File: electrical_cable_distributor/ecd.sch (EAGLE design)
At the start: 4 parts, among them X1 DG300-5.0-03P-13-00AH, X2 DG300-5.0-03P-13-00AH, X3 DG300-5.0-03P-13-00AH, X4 DG300-5.0-03P-13-00AH

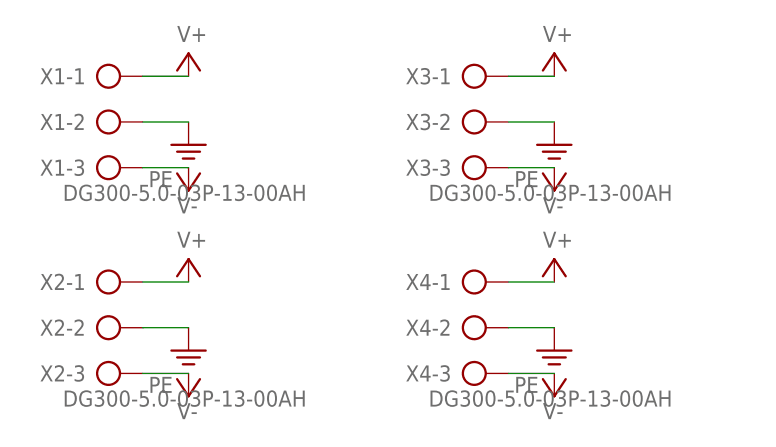
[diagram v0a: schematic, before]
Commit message: new design, with brick closer to each other
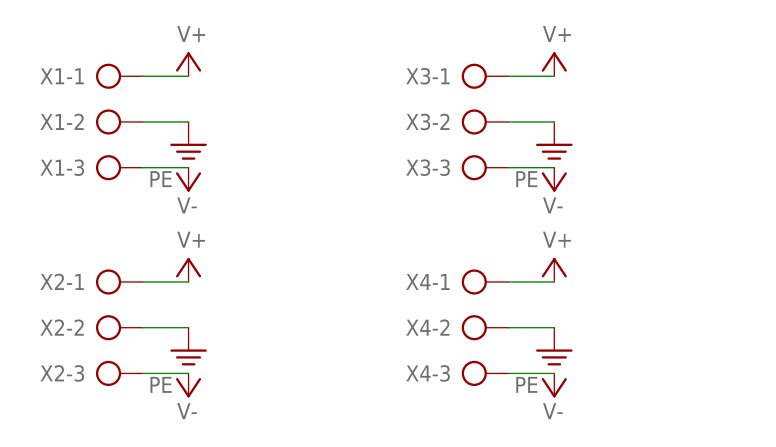
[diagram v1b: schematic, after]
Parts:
- X1, X2, X3, X4: value DG300-5.0-03P-13-00AH -> (none)
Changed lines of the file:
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@@
 </classes>
 <parts>
-<part name="X2" library="con-ptr500" deviceset="AK500/3" device="" value="DG300-5.0-03P-13-00AH"/>
-<part name="X1" library="con-ptr500" deviceset="AK500/3" device="" value="DG300-5.0-03P-13-00AH"/>
-<part name="X3" library="con-ptr500" deviceset="AK500/3" device="" value="DG300-5.0-03P-13-00AH"/>
-<part name="X4" library="con-ptr500" deviceset="AK500/3" device="" value="DG300-5.0-03P-13-00AH"/>
+<part name="X2" library="con-ptr500" deviceset="AK500/3" device=""/>
+<part name="X1" library="con-ptr500" deviceset="AK500/3" device=""/>
+<part name="X3" library="con-ptr500" deviceset="AK500/3" device=""/>
+<part name="X4" library="con-ptr500" deviceset="AK500/3" device=""/>
 <part name="SUPPLY1" library="supply2" deviceset="PE" device=""/>
 <part name="SUPPLY2" library="supply2" deviceset="PE" device=""/>
